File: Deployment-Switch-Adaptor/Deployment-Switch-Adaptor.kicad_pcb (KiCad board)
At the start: 2 copper layers, 13 x 11.5 mm, 2 parts, among them J1 Hirose_DF11-4DP-2DSA_2x02, J2 D2F-5L3

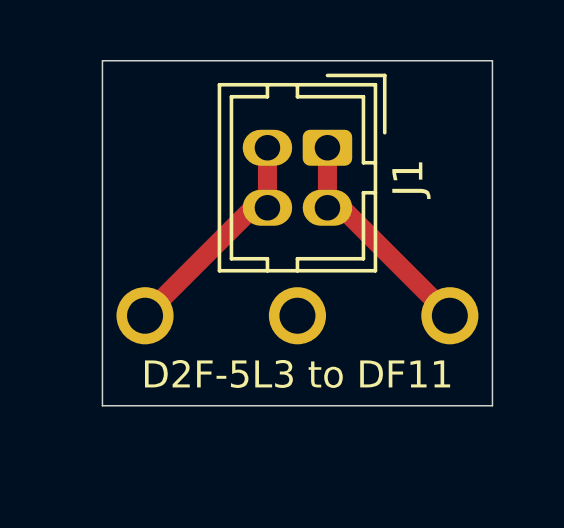
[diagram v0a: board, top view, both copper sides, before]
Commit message: Updated with official D2F-L Footprint
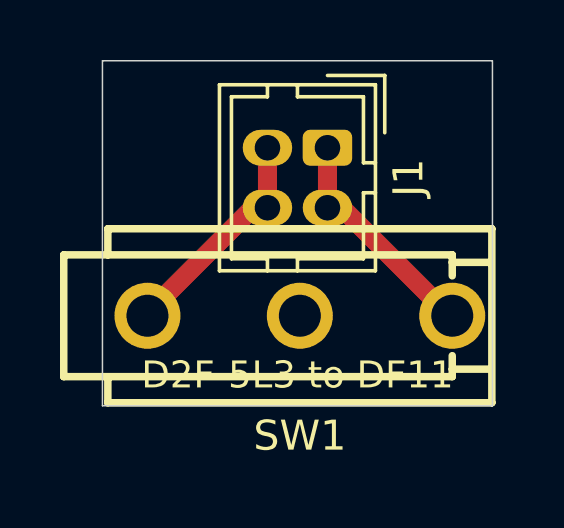
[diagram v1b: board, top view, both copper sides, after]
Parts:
- removed J2: D2F-5L3, proves-peripherals:D2F-5L3
- added SW1: D2F-L, easyeda2kicad:SW-TH_D2F-L, F.Cu at (163.1, 89.0)
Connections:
- J1 pad 1: V+ -> V-
- J1 pad 2: V- -> V+
- J1 pad 3: V+ -> V-
- J1 pad 4: V- -> V+
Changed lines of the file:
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@@
 	(net 1 "V-")
 	(net 2 "V+")
-	(net 3 "unconnected-(J2-Pin_2-Pad2)")
+	(net 3 "unconnected-(SW1-NO-Pad2)")
 	(footprint "Connector_Hirose:Hirose_DF11-4DP-2DSA_2x02_P2.00mm_Vertical"
 		(layer "F.Cu")
@@
 			(unlocked yes)
 			(layer "F.Fab")
+			(hide yes)
+			(effects
+				(font
+					(size 1.27 1.27)
+					(thickness 0.15)
+				)
+			)
+		)
+		(property "LCSC" "C2692098"
+			(at 0 0 0)
+			(layer "F.SilkS")
 			(hide yes)
 			(effects
@@
 			(remove_unused_layers no)
 			(roundrect_rratio 0.208333)
-			(net 2 "V+")
+			(net 1 "V-")
 			(pinfunction "Pin_1")
 			(pintype "passive")
@@
 			(layers "*.Cu" "*.Mask")
 			(remove_unused_layers no)
-			(net 1 "V-")
+			(net 2 "V+")
 			(pinfunction "Pin_2")
 			(pintype "passive")
@@
 			(layers "*.Cu" "*.Mask")
 			(remove_unused_layers no)
-			(net 2 "V+")
+			(net 1 "V-")
 			(pinfunction "Pin_3")
 			(pintype "passive")
@@
 			(layers "*.Cu" "*.Mask")
 			(remove_unused_layers no)
-			(net 1 "V-")
+			(net 2 "V+")
 			(pinfunction "Pin_4")
 			(pintype "passive")
@@
 		)
 	)
-	(footprint "proves-peripherals:D2F-5L3"
-		(layer "B.Cu")
-		(at 163 92 180)
-		(property "Reference" "J2"
-			(at -5 7 0)
+	(footprint "easyeda2kicad:SW-TH_D2F-L"
+		(layer "F.Cu")
+		(at 163.079999 89 180)
+		(property "Reference" "SW1"
+			(at 0 -4 0)
+			(layer "F.SilkS")
+			(effects
+				(font
+					(size 1 1)
+					(thickness 0.15)
+				)
+			)
+		)
+		(property "Value" "D2F-L"
+			(at 0 4 0)
+			(layer "F.Fab")
+			(effects
+				(font
+					(size 1 1)
+					(thickness 0.15)
+				)
+			)
+		)
+		(property "Datasheet" "https://lcsc.com/product-detail/Others_Omron-Electronics_D2F-L_Omron-Electronics-D2F-L_C231337.html"
+			(at 0 0 0)
+			(layer "F.Fab")
+			(hide yes)
+			(effects
+				(font
+					(size 1.27 1.27)
+					(thickness 0.15)
+				)
+			)
+		)
+		(property "Description" ""
+			(at 0 0 0)
+			(layer "F.Fab")
+			(hide yes)
+			(effects
+				(font
+					(size 1.27 1.27)
+					(thickness 0.15)
+				)
+			)
+		)
+		(property "LCSC Part" "C231337"
+			(at 0 0 180)
 			(unlocked yes)
-			(layer "B.SilkS")
+			(layer "F.Fab")
+			(hide yes)
 			(effects
 				(font
 					(size 1 1)
-					(thickness 0.1)
-				)
-				(justify mirror)
-			)
-		)
-		(property "Value" "D2F-5L3"
-			(at 0 -1 0)
-			(unlocked yes)
-			(layer "B.Fab")
-			(effects
-				(font
-					(size 1 1)
-					(thickness 0.15)
-				)
-				(justify mirror)
-			)
-		)
-		(property "Datasheet" ""
-			(at 0 0 0)
-			(unlocked yes)
-			(layer "B.Fab")
-			(hide yes)
-			(effects
-				(font
-					(size 1 1)
-					(thickness 0.15)
-				)
-				(justify mirror)
-			)
-		)
-		(property "Description" "Generic connector, single row, 01x03, script generated (kicad-library-utils/schlib/autogen/connector/)"
-			(at 0 0 0)
-			(unlocked yes)
-			(layer "B.Fab")
-			(hide yes)
-			(effects
-				(font
-					(size 1 1)
-					(thickness 0.15)
-				)
-				(justify mirror)
-			)
-		)
-		(property ki_fp_filters "Connector*:*_1x??_*")
+					(thickness 0.15)
+				)
+			)
+		)
 		(sheetname "/")
 		(sheetfile "Deployment-Switch-Adaptor.kicad_sch")
-		(attr smd)
-		(fp_poly
-			(pts
-				(xy -6.399999 5.9) (xy 6.399999 5.9) (xy 6.4 0.1) (xy -6.4 0.1)
-			)
-			(stroke
-				(width 0.1)
-				(type default)
+		(attr through_hole)
+		(fp_line
+			(start 7.87 2.03)
+			(end 7.87 -2.03)
+			(stroke
+				(width 0.25)
+				(type solid)
+			)
+			(layer "F.SilkS")
+		)
+		(fp_line
+			(start 7.87 -2.03)
+			(end -5.08 -2.03)
+			(stroke
+				(width 0.25)
+				(type solid)
+			)
+			(layer "F.SilkS")
+		)
+		(fp_line
+			(start 6.4 2.9)
+			(end 6.4 2.03)
+			(stroke
+				(width 0.25)
+				(type solid)
+			)
+			(layer "F.SilkS")
+		)
+		(fp_line
+			(start 6.4 2.9)
+			(end -6.4 2.9)
+			(stroke
+				(width 0.25)
+				(type solid)
+			)
+			(layer "F.SilkS")
+		)
+		(fp_line
+			(start 6.4 -2.9)
+			(end 6.4 -2.03)
+			(stroke
+				(width 0.25)
+				(type solid)
+			)
+			(layer "F.SilkS")
+		)
+		(fp_line
+			(start -5.079999 1.33)
+			(end -5.08 2.03)
+			(stroke
+				(width 0.25)
+				(type solid)
+			)
+			(layer "F.SilkS")
+		)
+		(fp_line
+			(start -5.08 2.03)
+			(end 7.87 2.03)
+			(stroke
+				(width 0.25)
+				(type solid)
+			)
+			(layer "F.SilkS")
+		)
+		(fp_line
+			(start -5.08 1.780001)
+			(end -6.35 1.78)
+			(stroke
+				(width 0.25)
+				(type solid)
+			)
+			(layer "F.SilkS")
+		)
+		(fp_line
+			(start -5.08 -1.780001)
+			(end -6.35 -1.78)
+			(stroke
+				(width 0.25)
+				(type solid)
+			)
+			(layer "F.SilkS")
+		)
+		(fp_line
+			(start -5.08 -2.03)
+			(end -5.079999 -1.33)
+			(stroke
+				(width 0.25)
+				(type solid)
+			)
+			(layer "F.SilkS")
+		)
+		(fp_line
+			(start -6.4 2.9)
+			(end -6.4 -2.9)
+			(stroke
+				(width 0.25)
+				(type solid)
+			)
+			(layer "F.SilkS")
+		)
+		(fp_line
+			(start -6.4 -2.9)
+			(end 6.4 -2.9)
+			(stroke
+				(width 0.25)
+				(type solid)
+			)
+			(layer "F.SilkS")
+		)
+		(fp_circle
+			(center -6.4 2.89)
+			(end -6.37 2.89)
+			(stroke
+				(width 0.06)
+				(type solid)
 			)
 			(fill no)
-			(layer "B.SilkS")
-		)
-		(fp_poly
-			(pts
-				(xy -6.6 6.1) (xy 6.6 6.1) (xy 6.6 -0.1) (xy -6.6 -0.1)
-			)
-			(stroke
-				(width 0.05)
-				(type default)
-			)
-			(fill no)
-			(layer "B.CrtYd")
+			(layer "F.Fab")
 		)
 		(fp_text user "${REFERENCE}"
-			(at 0 -2.5 0)
-			(unlocked yes)
-			(layer "B.Fab")
+			(at 0 0 0)
+			(layer "F.Fab")
 			(effects
 				(font
@@
 					(thickness 0.15)
 				)
-				(justify mirror)
 			)
 		)
 		(pad "1" thru_hole circle
-			(at -5.08 3 180)
-			(size 1.905 1.905)
-			(drill 1.2)
+			(at -5.079999 0 180)
+			(size 2.2 2.2)
+			(drill 1.399997)
+			(layers "*.Cu" "*.Mask")
+			(remove_unused_layers no)
+			(net 1 "V-")
+			(pinfunction "COM")
+			(pintype "unspecified")
+		)
+		(pad "2" thru_hole circle
+			(at 0 0 180)
+			(size 2.2 2.2)
+			(drill 1.399997)
+			(layers "*.Cu" "*.Mask")
+			(remove_unused_layers no)
+			(net 3 "unconnected-(SW1-NO-Pad2)")
+			(pinfunction "NO")
+			(pintype "unspecified+no_connect")
+		)
+		(pad "3" thru_hole circle
+			(at 5.079999 0 180)
+			(size 2.2 2.2)
+			(drill 1.399997)
 			(layers "*.Cu" "*.Mask")
 			(remove_unused_layers no)
 			(net 2 "V+")
-			(pinfunction "Common")
-			(pintype "passive")
-		)
-		(pad "2" thru_hole circle
-			(at 0 3 180)
-			(size 1.905 1.905)
-			(drill 1.2)
-			(layers "*.Cu" "*.Mask")
-			(remove_unused_layers no)
-			(net 3 "unconnected-(J2-Pin_2-Pad2)")
-			(pinfunction "Pin_2")
-			(pintype "passive+no_connect")
-		)
-		(pad "3" thru_hole circle
-			(at 5.08 3 180)
-			(size 1.905 1.905)
-			(drill 1.2)
-			(layers "*.Cu" "*.Mask")
-			(remove_unused_layers no)
-			(net 1 "V-")
-			(pinfunction "Pin_3")
-			(pintype "passive")
+			(pinfunction "NC")
+			(pintype "unspecified")
 		)
 		(embedded_fonts no)
+		(model "${EASYEDA2KICAD}/easyeda2kicad.3dshapes/SW-TH_D2F-L-L13.0-W5.8-H11.6-P5.08.wrl"
+			(offset
+				(xyz 0.1 -0 0)
+			)
+			(scale
+				(xyz 1 1 1)
+			)
+			(rotate
+				(xyz 0 0 0)
+			)
+		)
 	)
 	(gr_rect
@@
 	)
 	(segment
+		(start 164 85.400001)
+		(end 164.480001 85.400001)
+		(width 0.635)
+		(layer "F.Cu")
+		(net 1)
+	)
+	(segment
+		(start 164.480001 85.400001)
+		(end 168.08 89)
+		(width 0.635)
+		(layer "F.Cu")
+		(net 1)
+	)
+	(segment
+		(start 164 83.4)
+		(end 164 85.400001)
+		(width 0.635)
+		(layer "F.Cu")
+		(net 1)
+	)
+	(segment
 		(start 162 85.4)
 		(end 161.52 85.4)
 		(width 0.635)
 		(layer "F.Cu")
-		(net 1)
+		(net 2)
 	)
 	(segment
@@
 		(width 0.635)
 		(layer "F.Cu")
-		(net 1)
+		(net 2)
 	)
 	(segment
@@
 		(width 0.635)
 		(layer "F.Cu")
-		(net 1)
+		(net 2)
 	)
 	(segment
@@
 		(width 0.635)
 		(layer "F.Cu")
-		(net 1)
-	)
-	(segment
-		(start 164 85.400001)
-		(end 164.480001 85.400001)
-		(width 0.635)
-		(layer "F.Cu")
-		(net 2)
-	)
-	(segment
-		(start 164.480001 85.400001)
-		(end 168.08 89)
-		(width 0.635)
-		(layer "F.Cu")
-		(net 2)
-	)
-	(segment
-		(start 164 83.4)
-		(end 164 85.400001)
-		(width 0.635)
-		(layer "F.Cu")

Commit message: Adjusted the Deploy Edge Cits
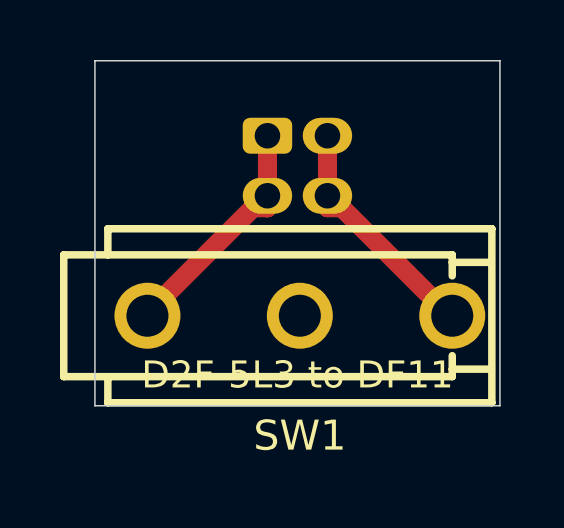
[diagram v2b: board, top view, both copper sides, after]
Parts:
- J1: moved to B.Cu
- moved J1 2.04 mm to (162.0, 83.0)
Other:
- board size 13 x 11.5 mm -> 13.5 x 11.5 mm
